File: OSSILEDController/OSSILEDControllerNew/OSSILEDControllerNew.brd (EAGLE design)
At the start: 94 x 88 mm, 80 parts, among them Q1 NX-3215, U1 MSP430F2132, U2 OPA2347, U3 MAX4376, U4 LM7321, U5 MAX1682, U6 TPS3838, U7 MAX890L, U8 MCP1700_SOT23, X1 ESQ-126-38-G-D, X2 5268-03, X3 5268-03, X4 JTAG10PINMINI-H, X5 ICCON_POWERCON, X6 ICCON_POWERCON, X7 WEIDMULLER

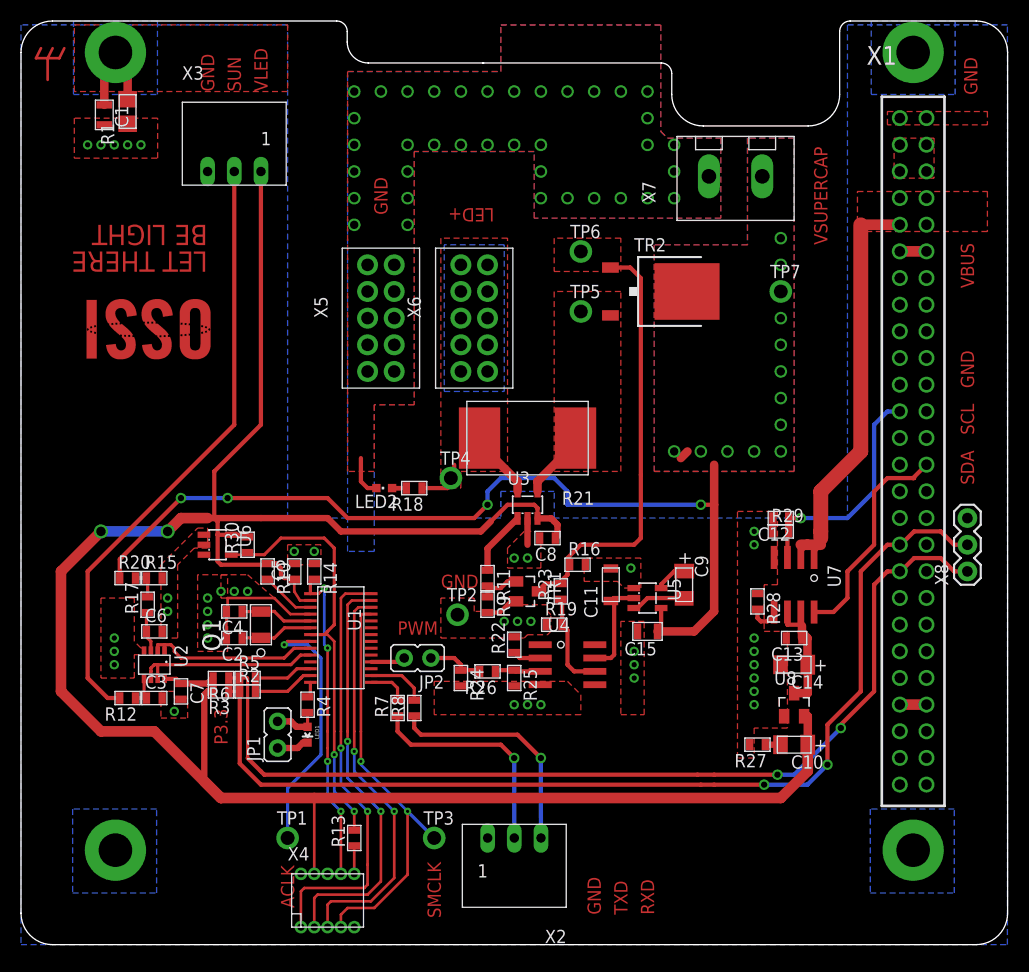
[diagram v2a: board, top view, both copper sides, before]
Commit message: schematics renumbered
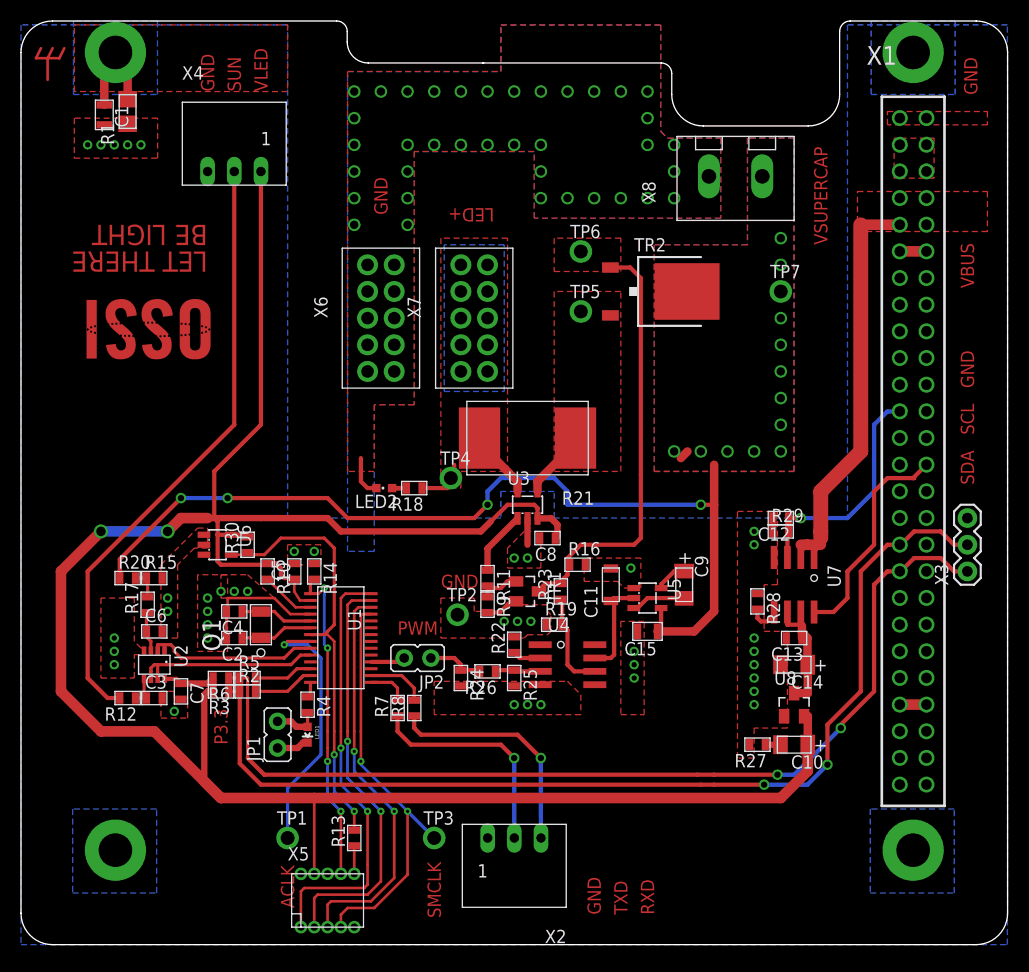
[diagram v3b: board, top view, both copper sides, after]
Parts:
- X3: value 5268-03 -> (none); device OSSI:5268-03 -> OSSI:1X03
- X4: value JTAG10PINMINI-H -> 5268-03; device OSSI:M50-3200545 -> OSSI:5268-03
- X5: value ICCON_POWERCON -> JTAG10PINMINI-H; device OSSI:ICCON6643220-1 -> OSSI:M50-3200545
- X7: value WEIDMULLER -> ICCON_POWERCON; device OSSI:WEIDMULLER1760490000 -> OSSI:ICCON6643220-1
- X8: value (none) -> WEIDMULLER; device OSSI:1X03 -> OSSI:WEIDMULLER1760490000
- moved X3 79.6 mm to (90.2, 35.6), turned to 90 degrees
- moved X4 70.0 mm to (20.3, 73.7)
- moved X5 55.7 mm to (29.2, 4.21)
- moved X8 43.6 mm to (68.1, 73.2), turned to 0 degrees
- moved X7 28.3 mm to (43.2, 59.7)
- moved X6 8.89 mm to (34.3, 59.7)
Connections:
- net 3.3VLED: now also X4.1, X5.4; no longer X3.1, X4.4
- net GND: now also X4.3, X6.1, X6.10, X6.2, X6.3, X6.4, X6.5, X6.6, X6.7, X6.8, X6.9, X8.2; no longer X4.9, X5.1, X5.10, X5.2, X5.3, X5.4, X5.5, X5.6, X5.7, X5.8, X7.2, X8.3
- net LED_SCL: now also X3.2; no longer X8.2
- net LED_SDA: now also X3.1; no longer X8.1
- net N$12: now also X7.1, X7.10, X7.2, X7.3, X7.4, X7.5, X7.6, X7.7, X7.8, X7.9; no longer X6.1, X6.10, X6.2, X6.3, X6.4, X6.5, X6.6, X6.7, X6.8, X6.9
- net N$15: now also X5.3; no longer X4.3
- net N$3: now also X5.1; no longer X4.1
- net N$31: now also X5.5; no longer X4.5
- net N$32: now also X5.10; no longer X4.10
- net SMCLK_OUT: now also X5.7; no longer X4.7
- net SUN: now also X4.2; no longer X3.2
- net TEST: now also X5.8; no longer X4.8
- net VSUPERCAP: now also X8.1; no longer X7.1
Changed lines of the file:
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@@
 <element name="R11" library="OSSI" package="R0603(1608)" value="9.1k" x="44.45" y="34.925" rot="R270"/>
 <element name="R9" library="OSSI" package="R0603(1608)" value="6.2k" x="44.45" y="32.385" rot="R270"/>
-<element name="X3" library="OSSI" package="5268-03" value="5268-03" x="20.32" y="73.66"/>
-<element name="X6" library="OSSI" package="ICCON6643220-1" value="ICCON_POWERCON" x="43.18" y="59.69"/>
-<element name="X5" library="OSSI" package="ICCON6643220-1" value="ICCON_POWERCON" x="34.29" y="59.69"/>
-<element name="X7" library="OSSI" package="WEIDMULLER1760490000" value="WEIDMULLER" x="68.08" y="73.2"/>
-<element name="X4" library="OSSI" package="M50-3200545" value="JTAG10PINMINI-H" x="29.21" y="4.2075"/>
+<element name="X4" library="OSSI" package="5268-03" value="5268-03" x="20.32" y="73.66"/>
+<element name="X7" library="OSSI" package="ICCON6643220-1" value="ICCON_POWERCON" x="43.18" y="59.69"/>
+<element name="X6" library="OSSI" package="ICCON6643220-1" value="ICCON_POWERCON" x="34.29" y="59.69"/>
+<element name="X8" library="OSSI" package="WEIDMULLER1760490000" value="WEIDMULLER" x="68.08" y="73.2"/>
+<element name="X5" library="OSSI" package="M50-3200545" value="JTAG10PINMINI-H" x="29.21" y="4.2075"/>
 <element name="R13" library="OSSI" package="R0603(1608)" value="4.7k" x="31.75" y="10.16" rot="R90"/>
 <element name="X2" library="OSSI" package="5268-03" value="5268-03" x="47" y="10.16" rot="R180"/>
@@
 <element name="R1" library="OSSI" package="WSL1206" value="511" x="10.16" y="79.375" rot="R90"/>
 <element name="C1" library="OSSI" package="C0805(2012)" value="" x="7.9375" y="79.0575" rot="R270"/>
-<element name="X8" library="OSSI" package="1X03" value="" x="90.17" y="35.56" rot="R90"/>
+<element name="X3" library="OSSI" package="1X03" value="" x="90.17" y="35.56" rot="R90"/>
 </elements>
 <signals>
@@
 <contactref element="TR1" pad="2"/>
 <contactref element="R9" pad="2"/>
-<contactref element="X3" pad="3"/>
-<contactref element="X5" pad="10"/>
-<contactref element="X5" pad="6"/>
-<contactref element="X5" pad="9"/>
-<contactref element="X5" pad="8"/>
-<contactref element="X5" pad="7"/>
-<contactref element="X5" pad="1"/>
-<contactref element="X5" pad="2"/>
-<contactref element="X5" pad="3"/>
-<contactref element="X5" pad="4"/>
-<contactref element="X5" pad="5"/>
-<contactref element="X7" pad="2"/>
+<contactref element="X4" pad="3"/>
+<contactref element="X6" pad="10"/>
+<contactref element="X6" pad="6"/>
+<contactref element="X6" pad="9"/>
+<contactref element="X6" pad="8"/>
+<contactref element="X6" pad="7"/>
+<contactref element="X6" pad="1"/>
+<contactref element="X6" pad="2"/>
+<contactref element="X6" pad="3"/>
+<contactref element="X6" pad="4"/>
+<contactref element="X6" pad="5"/>
+<contactref element="X8" pad="2"/>
 <polygon width="0.254" layer="1" thermals="no">
 <vertex x="66.675" y="76.835"/>
@@
 <vertex x="93.98" y="87.63"/>
 </polygon>
-<contactref element="X4" pad="9"/>
+<contactref element="X5" pad="9"/>
 <contactref element="X2" pad="1"/>
 <wire x1="44.45" y1="31.635" x2="45.605" y2="31.635" width="0.4064" layer="1"/>
@@
 <vertex x="82.55" y="78.105"/>
 </polygon>
-<contactref element="X8" pad="3"/>
+<contactref element="X3" pad="3"/>
 <via x="31.75" y="71.12" extent="1-16" drill="0.8"/>
 <via x="31.75" y="68.58" extent="1-16" drill="0.8"/>
@@
 <contactref element="U5" pad="4"/>
 <contactref element="C15" pad="1"/>
-<contactref element="X7" pad="1"/>
+<contactref element="X8" pad="1"/>
 <polygon width="0.254" layer="1" thermals="no">
 <vertex x="69.215" y="76.835"/>
@@
 <wire x1="83.82" y1="38.1" x2="83.74" y2="38.1" width="0.4064" layer="1"/>
 <wire x1="83.74" y1="38.1" x2="83.73" y2="38.11" width="0.4064" layer="1"/>
-<contactref element="X8" pad="2"/>
+<contactref element="X3" pad="2"/>
 <wire x1="83.82" y1="38.1" x2="85.09" y2="39.37" width="0.4064" layer="1"/>
 <wire x1="85.09" y1="39.37" x2="87.63" y2="39.37" width="0.4064" layer="1"/>
@@
 <via x="78.105" y="20.6375" extent="1-16" drill="0.6"/>
 <wire x1="83.72" y1="35.56" x2="83.73" y2="35.57" width="0.4064" layer="1"/>
-<contactref element="X8" pad="1"/>
+<contactref element="X3" pad="1"/>
 <wire x1="83.73" y1="35.57" x2="83.83" y2="35.57" width="0.4064" layer="1"/>
 <wire x1="83.83" y1="35.57" x2="85.09" y2="36.83" width="0.4064" layer="1"/>
@@
 <contactref element="U3" pad="3"/>
 <contactref element="C8" pad="1"/>
-<contactref element="X3" pad="1"/>
-<contactref element="X4" pad="4"/>
+<contactref element="X4" pad="1"/>
+<contactref element="X5" pad="4"/>
 <wire x1="74.61" y1="21.76" x2="74.96" y2="21.76" width="0.8128" layer="1"/>
 <wire x1="74.96" y1="21.76" x2="74.96" y2="19.05" width="0.8128" layer="1"/>
@@
 <contactref element="U1" pad="1"/>
 <contactref element="R14" pad="2"/>
-<contactref element="X4" pad="8"/>
+<contactref element="X5" pad="8"/>
 <wire x1="27.572" y1="33.439" x2="27.572" y2="34.557" width="0.3048" layer="1"/>
 <wire x1="27.572" y1="34.557" x2="27.94" y2="34.925" width="0.3048" layer="1"/>
@@
 <signal name="SMCLK_OUT">
 <contactref element="U1" pad="25"/>
-<contactref element="X4" pad="7"/>
+<contactref element="X5" pad="7"/>
 <wire x1="33.3721" y1="31.4891" x2="32.4416" y2="31.4891" width="0.254" layer="1"/>
 <wire x1="32.4416" y1="31.4891" x2="32.385" y2="31.4325" width="0.254" layer="1"/>
@@
 <contactref element="U3" pad="5"/>
 <contactref element="R18" pad="1"/>
-<contactref element="X6" pad="6"/>
-<contactref element="X6" pad="7"/>
-<contactref element="X6" pad="8"/>
-<contactref element="X6" pad="9"/>
-<contactref element="X6" pad="10"/>
-<contactref element="X6" pad="5"/>
-<contactref element="X6" pad="4"/>
-<contactref element="X6" pad="3"/>
-<contactref element="X6" pad="2"/>
-<contactref element="X6" pad="1"/>
+<contactref element="X7" pad="6"/>
+<contactref element="X7" pad="7"/>
+<contactref element="X7" pad="8"/>
+<contactref element="X7" pad="9"/>
+<contactref element="X7" pad="10"/>
+<contactref element="X7" pad="5"/>
+<contactref element="X7" pad="4"/>
+<contactref element="X7" pad="3"/>
+<contactref element="X7" pad="2"/>
+<contactref element="X7" pad="1"/>
 <polygon width="0.254" layer="1" thermals="no">
 <vertex x="40.005" y="67.31"/>
@@
 <signal name="SUN">
 <contactref element="R12" pad="2"/>
-<contactref element="X3" pad="2"/>
+<contactref element="X4" pad="2"/>
 <wire x1="9.41" y1="23.495" x2="8.255" y2="23.495" width="0.4064" layer="1"/>
 <wire x1="8.255" y1="23.495" x2="6.35" y2="25.4" width="0.4064" layer="1"/>
@@
 <signal name="N$3">
 <contactref element="U1" pad="28"/>
-<contactref element="X4" pad="1"/>
+<contactref element="X5" pad="1"/>
 <wire x1="33.3721" y1="33.439" x2="30.899" y2="33.439" width="0.254" layer="1"/>
 <wire x1="30.899" y1="33.439" x2="30.48" y2="33.02" width="0.254" layer="1"/>
@@
 <signal name="N$15">
 <contactref element="U1" pad="27"/>
-<contactref element="X4" pad="3"/>
+<contactref element="X5" pad="3"/>
 <wire x1="33.3721" y1="32.789" x2="31.519" y2="32.789" width="0.254" layer="1"/>
 <wire x1="31.519" y1="32.789" x2="31.115" y2="32.385" width="0.254" layer="1"/>
@@
 <signal name="N$31">
 <contactref element="U1" pad="26"/>
-<contactref element="X4" pad="5"/>
+<contactref element="X5" pad="5"/>
 <wire x1="33.3721" y1="32.139" x2="32.139" y2="32.139" width="0.254" layer="1"/>
 <wire x1="32.139" y1="32.139" x2="31.75" y2="31.75" width="0.254" layer="1"/>
@@
 <signal name="N$32">
 <contactref element="R13" pad="1"/>
-<contactref element="X4" pad="10"/>
+<contactref element="X5" pad="10"/>
 <wire x1="31.75" y1="6.7475" x2="31.75" y2="9.41" width="0.254" layer="1"/>
 </signal>
